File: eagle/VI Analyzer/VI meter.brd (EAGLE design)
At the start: 101.7 x 73.7 mm, 63 parts, among them IC2 E50D, IC3 LM358D, J4 MF-CON-MICROUSB-RIGHT, SW2 Load Switch, SW3 Hi Res, SW4 Hi Res

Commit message: ADD: Hi res current reading from ads1115
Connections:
- net I-OUT renamed ACS-OUT
- net N$36 renamed POT_OFFSET
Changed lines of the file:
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@@
 <wire x1="43.688" y1="43.053" x2="44.955" y2="43.053" width="0.1524" layer="1"/>
 </signal>
-<signal name="I-OUT">
+<signal name="ACS-OUT">
 <contactref element="U$5" pad="3"/>
 <contactref element="U$5" pad="4"/>
@@
 <wire x1="48.26" y1="41.91" x2="50.8" y2="44.45" width="0.1524" layer="16"/>
 </signal>
-<signal name="N$36">
+<signal name="POT_OFFSET">
 <contactref element="R24" pad="2"/>
 <contactref element="R27" pad="3"/>

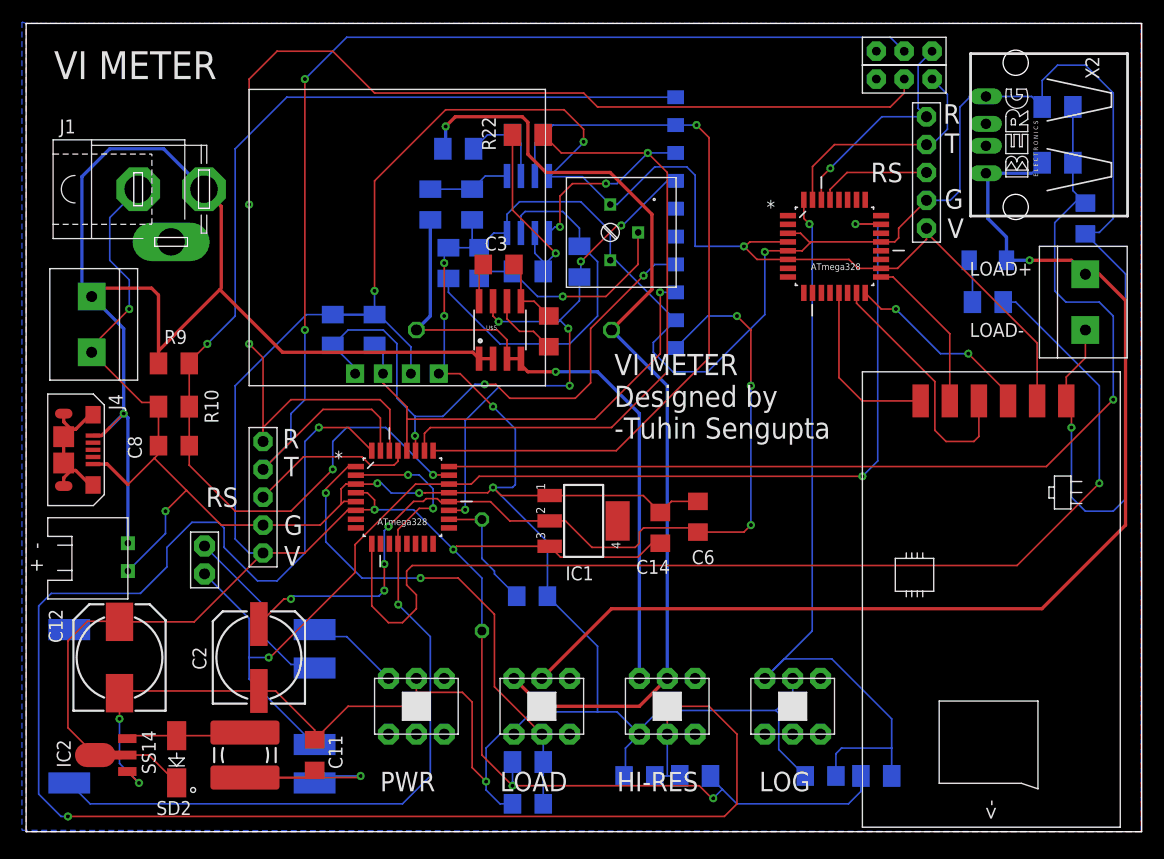
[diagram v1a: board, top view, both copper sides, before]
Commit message: Fix: moved the shunt to the lower side, single channel amp instead of differential
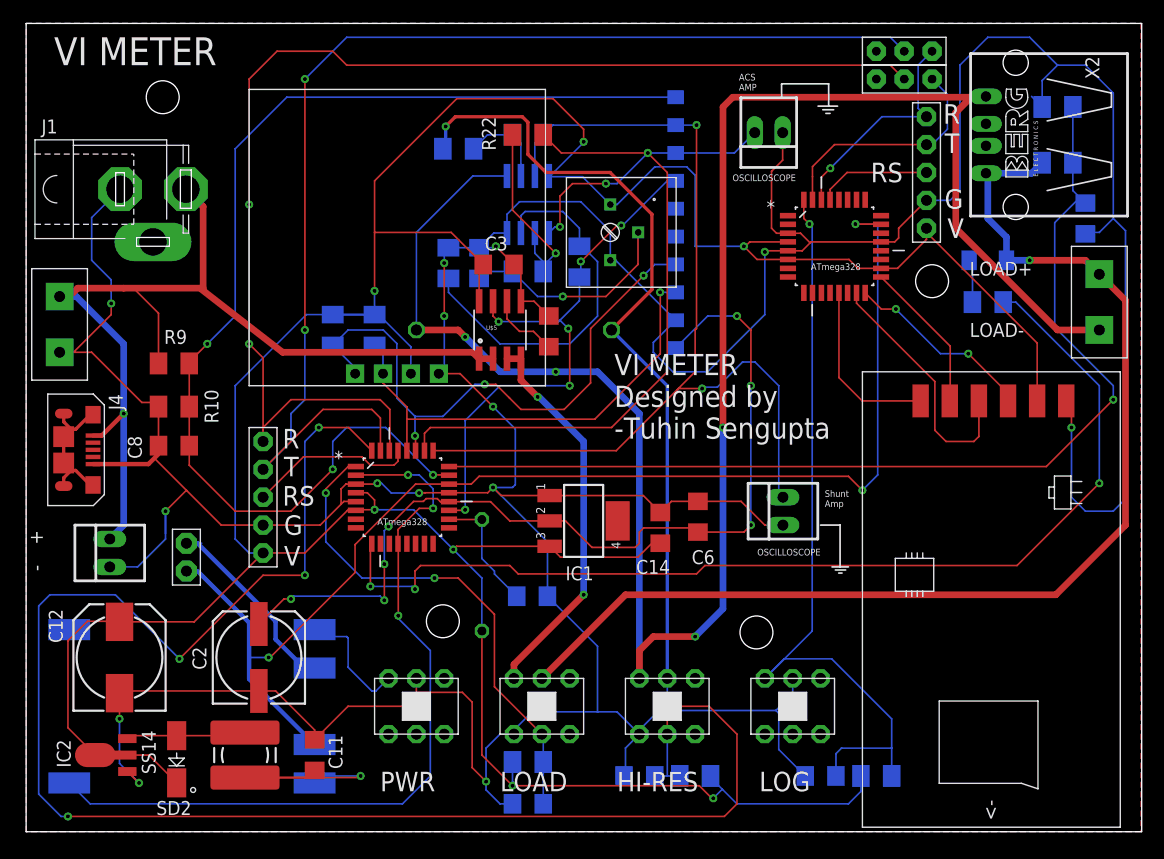
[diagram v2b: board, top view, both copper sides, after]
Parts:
- removed R7: 1K, rcl:M1206
- removed R8: 330K, rcl:M1206
- removed U$8: PH-JST-2-ANGLE, dragCustom:PH-JST-2-ANGLE
- added OSCILLOSCOPE, X1: 22-23-2021, con-molex:22-23-2021
- added X3: (no value), con-molex:22-23-2021
- moved U$7 1.67 mm to (13.3, 21.2)
- moved J1 1.65 mm to (10.3, 56.0)
- moved U$1 1.65 mm to (1.78, 43.7)
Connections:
- removed net ACS-OUT: R4.1, R7.2, SW3.1, U$5.3, U$5.4
- removed net GND2: C3.2, C4.2, U$5.5
- removed net N$5: IC3.5, R7.1, R8.1
- removed net OUT+\: R4.2, R6.2, SW2.1, SW3.2
- removed net VCC2: C3.1, U$5.8
- new net LOAD-: IC3.5, R4.1, SW3.1, U$3.1, X2.4
- new net N$6: SW2.1, U$5.3, U$5.4
- net AMPED_ACS_OUT: now also X3.2
- net GND: now also C3.2, C4.2, OSCILLOSCOPE.1, R4.2, R6.2, SW3.2, U$5.5, X1.1, X3.1; no longer R8.2, U$3.1, U$8.1, X2.4
- net HI_RES_CURRENT: now also OSCILLOSCOPE.2
- net IN+: now also X1.2; no longer U$8.2
- net VCC: now also C3.1, U$5.8
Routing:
- net LOAD-: track 0.00 -> 179.3 mm, vias 0 -> 4
- net GND: track 435.3 -> 551.5 mm, vias 13 -> 15
- net OUT+\: track 88.7 -> 0.00 mm, vias 1 -> 0
- net ACS-OUT: track 59.5 -> 0.00 mm, vias 1 -> 0
- net N$6: track 0.00 -> 35.5 mm, vias 0 -> 2
- net IN+: track 113.8 -> 90.1 mm
- net HI_RES_CURRENT: track 68.7 -> 89.1 mm, vias 1 -> 2
- net VCC: track 301.5 -> 317.0 mm
- net AMPED_ACS_OUT: track 73.1 -> 81.1 mm
- net N$5: track 7.48 -> 0.00 mm
- net GND2: track 6.71 -> 0.00 mm
- net PULL_UP: track 102.1 -> 97.0 mm, vias 1 -> 3
- net VCC2: track 3.51 -> 0.00 mm
- net BAT+: track 111.7 -> 115.0 mm
- net BAT-: track 16.4 -> 19.2 mm
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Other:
- board text added: "ACS AMP"
- board text added: "BAT+"
- board text added: "BAT-"
- board text added: "OSCILLOSCOPE"
- board text added: "Shunt Amp"

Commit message: Edit: fixed source voltage, can be improved with more granular peice-wise equations
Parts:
- added R1: 10K, rcl:M1206
- added U$8: BERG_3, dragCustom:BERG_3
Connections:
- new net N$5: R12.1, U$8.G
- net MRST: now also R1.2
- net OUT+: now also U$8.F; no longer R12.1
- net VCC: now also R1.1
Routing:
- net N$5: track 0.00 -> 67.4 mm, vias 0 -> 1
- net VCC: track 317.0 -> 321.5 mm, vias 7 -> 8
- net MRST: track 15.2 -> 19.4 mm
- net OUT+: track 106.4 -> 103.1 mm
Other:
- board text added: "O/P Sense"
